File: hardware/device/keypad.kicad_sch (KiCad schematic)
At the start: 49 parts, among them SW1 TRIG1, SW10 TRIG10, SW11 TRIG11, SW12 TRIG12, SW13 TRIG13, SW14 TRIG14, SW15 TRIG15, SW16 TRIG16, SW2 TRIG2, SW3 TRIG3, SW4 TRIG4, SW5 TRIG5, SW6 TRIG6, SW7 TRIG7, SW8 TRIG8, SW9 TRIG9, U10 TRIG9, U11 TRIG13, U12 TRIG10, U13 TRIG14, U14 TRIG11, U15 TRIG15, U16 TRIG12, U17 TRIG16, U2 TRIG1, U25 TCA8418RTWR, U3 TRIG2, U4 TRIG3, U5 TRIG4, U6 TRIG8, U7 TRIG7, U8 TRIG6, U9 TRIG5

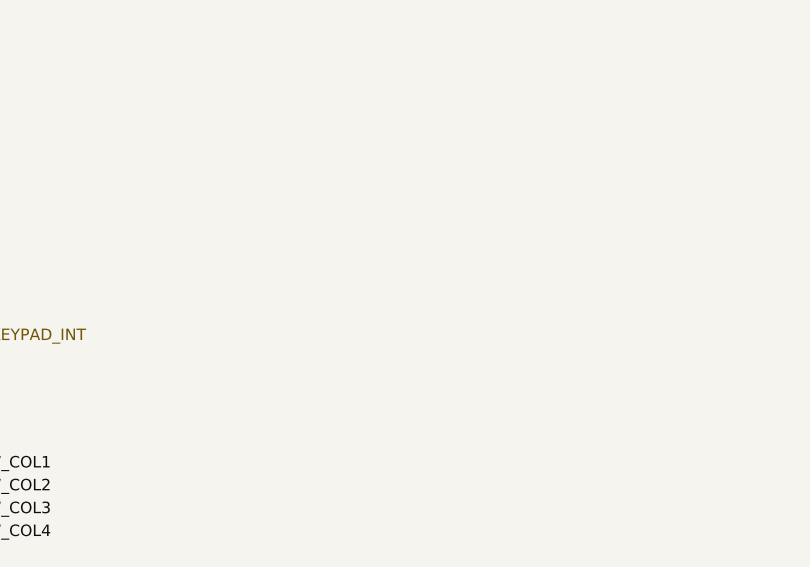
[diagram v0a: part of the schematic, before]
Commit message: feat: project organization, add knob, pcb layout, and 3d models
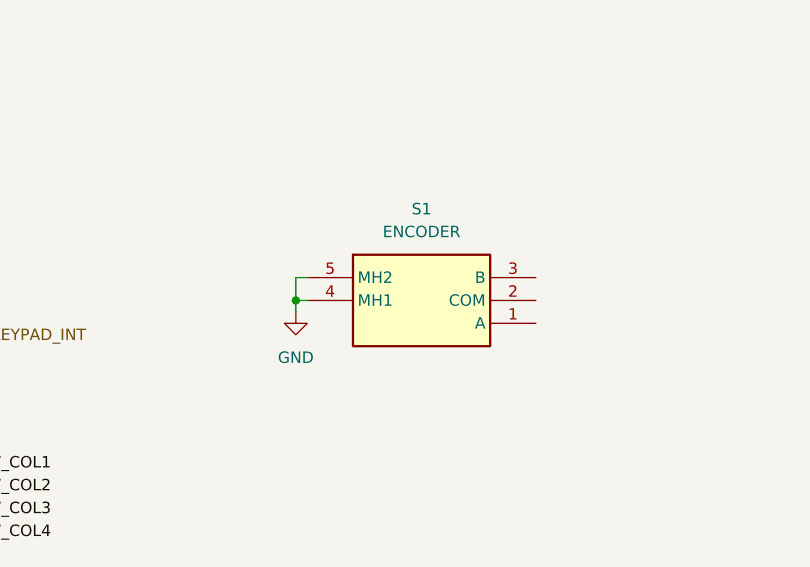
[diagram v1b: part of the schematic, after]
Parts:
- added S1: ENCODER, pocket_synth:2416191-1, symbol pocket_synth:2416191-1
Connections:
- net GND: now also S1.4 (MH1), S1.5 (MH2)

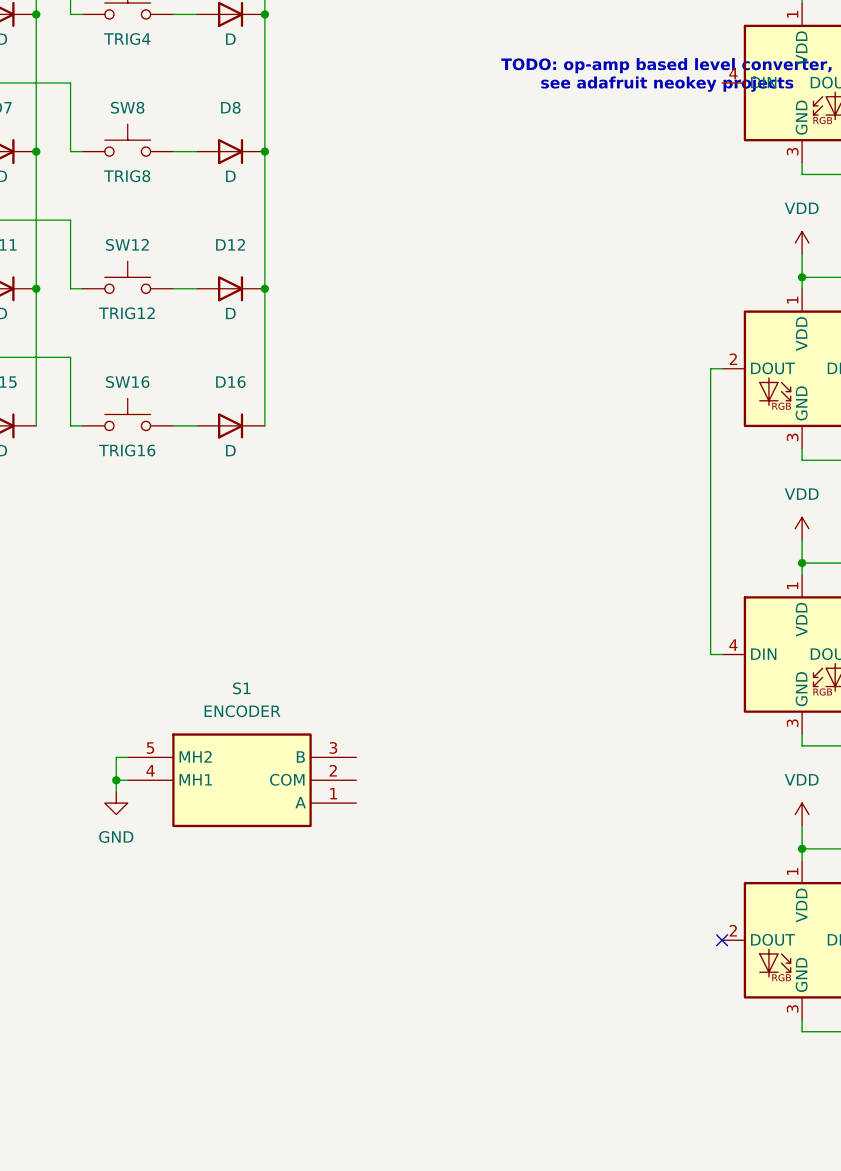
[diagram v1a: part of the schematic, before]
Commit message: feat: various scroll wheel layout changes
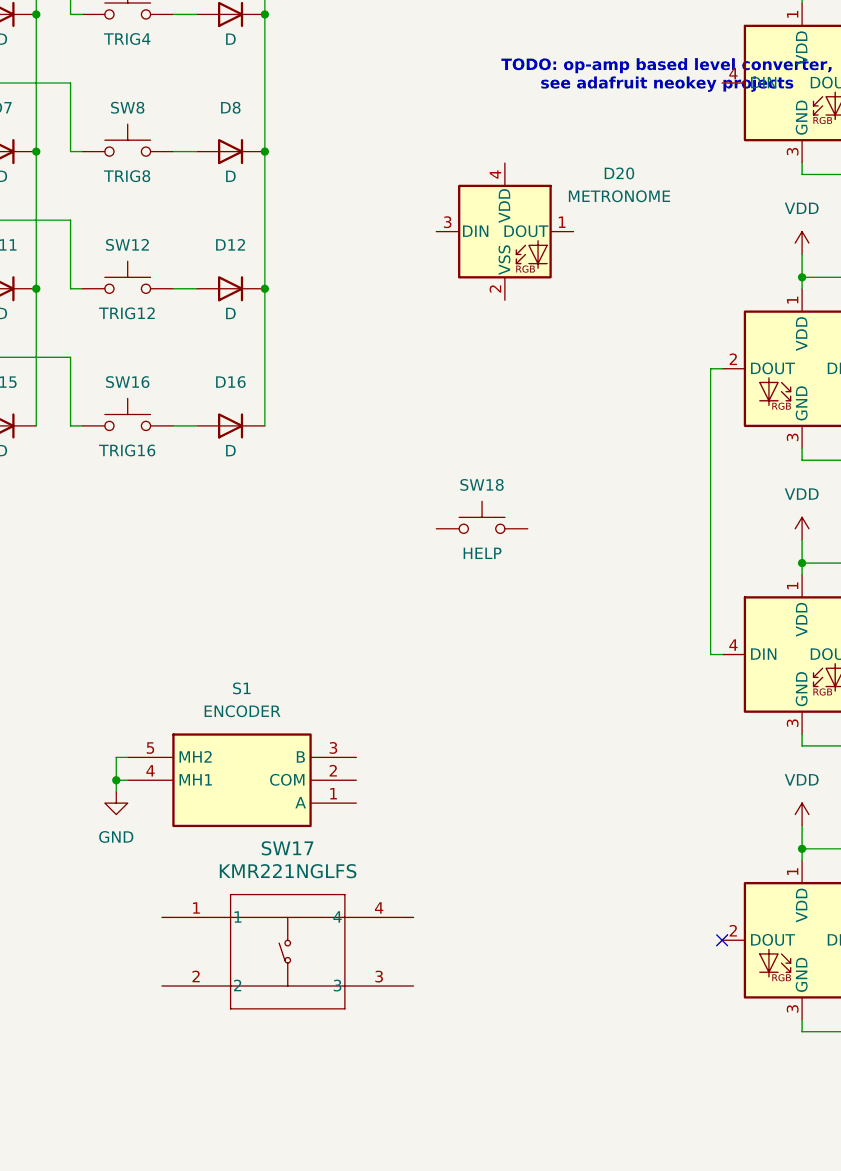
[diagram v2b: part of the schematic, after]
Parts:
- added D20: METRONOME, LED_SMD:LED_SK6812MINI_PLCC4_3.5x3.5mm_P1.75mm, symbol LED:SK6812MINI
- added SW17: KMR221NGLFS, pocket_synth:KMR221_CNK, symbol pocket_synth:KMR221NGLFS
- added SW18: HELP, Button_Switch_SMD:SW_SPST_EVQQ2, symbol Switch:SW_Push
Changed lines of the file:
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@@
+	(symbol
+		(lib_id "Switch:SW_Push")
+		(at 156.21 91.44 0)
+		(unit 1)
+		(exclude_from_sim no)
+		(in_bom yes)
+		(on_board yes)
+		(dnp no)
+		(property "Reference" "SW18"
+			(at 156.21 86.614 0)
+			(effects
+				(font
+					(size 1.27 1.27)
+				)
+			)
+		)
+		(property "Value" "HELP"
+			(at 156.21 93.472 0)
+			(effects
+				(font
+					(size 1.27 1.27)
+				)
+				(justify top)
+			)
+		)
+		(property "Footprint" "Button_Switch_SMD:SW_SPST_EVQQ2"
+			(at 156.21 86.36 0)
+			(effects
+				(font
+					(size 1.27 1.27)
+				)
+				(hide yes)
+			)
+		)
+		(property "Datasheet" "~"
+			(at 156.21 86.36 0)
+			(effects
+				(font
+					(size 1.27 1.27)
+				)
+				(hide yes)
+			)
+		)
+		(property "Description" "Push button switch, generic, two pins"
+			(at 156.21 91.44 0)
+			(effects
+				(font
+					(size 1.27 1.27)
+				)
+				(hide yes)
+			)
+		)
+		(property "JLC" ""
+			(at 156.21 91.44 0)
+			(effects
+				(font
+					(size 1.27 1.27)
+				)
+			)
+		)
+		(pin "1"
+		)
+		(pin "2"
+		)
+		(instances
+			(project "pocket_synth"
+				(path "/485383b8-00f4-4405-b270-de249939cff4/7f1ac839-494f-4521-b63e-5606a3cb7bc9"
+					(reference "SW18")
+					(unit 1)
+				)
+			)
+		)
+	)
 	(symbol
 		(lib_id "Switch:SW_Push")
@@
 	)
 	(symbol
+		(lib_id "LED:SK6812MINI")
+		(at 158.75 58.42 0)
+		(unit 1)
+		(exclude_from_sim no)
+		(in_bom yes)
+		(on_board yes)
+		(dnp no)
+		(fields_autoplaced yes)
+		(property "Reference" "D20"
+			(at 171.45 51.9998 0)
+			(effects
+				(font
+					(size 1.27 1.27)
+				)
+			)
+		)
+		(property "Value" "METRONOME"
+			(at 171.45 54.5398 0)
+			(effects
+				(font
+					(size 1.27 1.27)
+				)
+			)
+		)
+		(property "Footprint" "LED_SMD:LED_SK6812MINI_PLCC4_3.5x3.5mm_P1.75mm"
+			(at 160.02 66.04 0)
+			(effects
+				(font
+					(size 1.27 1.27)
+				)
+				(justify left top)
+				(hide yes)
+			)
+		)
+		(property "Datasheet" "https://cdn-shop.adafruit.com/product-files/2686/SK6812MINI_REV.01-1-2.pdf"
+			(at 161.29 67.945 0)
+			(effects
+				(font
+					(size 1.27 1.27)
+				)
+				(justify left top)
+				(hide yes)
+			)
+		)
+		(property "Description" "RGB LED with integrated controller"
+			(at 158.75 58.42 0)
+			(effects
+				(font
+					(size 1.27 1.27)
+				)
+				(hide yes)
+			)
+		)
+		(pin "3"
+		)
+		(pin "4"
+		)
+		(pin "2"
+		)
+		(pin "1"
+		)
+		(instances
+			(project ""
+				(path "/485383b8-00f4-4405-b270-de249939cff4/7f1ac839-494f-4521-b63e-5606a3cb7bc9"
+					(reference "D20")
+					(unit 1)
+				)
+			)
+		)
+	)
+	(symbol
 		(lib_id "power:VDD")
 		(at 191.77 29.21 0)
@@
 					(unit 1)
 				)
+			)
+		)
+	)
+	(symbol
+		(lib_id "pocket_synth:KMR221NGLFS")
+		(at 120.65 134.62 0)
+		(unit 1)
+		(exclude_from_sim no)
+		(in_bom yes)
+		(on_board yes)
+		(dnp no)
+		(fields_autoplaced yes)
+		(property "Reference" "SW17"
+			(at 134.62 127 0)
+			(effects
+				(font
+					(size 1.524 1.524)
+				)
+			)
+		)
+		(property "Value" "KMR221NGLFS"
+			(at 134.62 129.54 0)
+			(effects
+				(font
+					(size 1.524 1.524)
+				)
+			)
+		)
+		(property "Footprint" "pocket_synth:KMR221_CNK"
+			(at 120.65 134.62 0)
+			(effects
+				(font
+					(size 1.27 1.27)
+					(italic yes)
+				)
+				(hide yes)
+			)
+		)
+		(property "Datasheet" "KMR221NGLFS"
+			(at 120.65 134.62 0)
+			(effects
+				(font
+					(size 1.27 1.27)
+					(italic yes)
+				)
+				(hide yes)
+			)
+		)
+		(property "Description" ""
+			(at 120.65 134.62 0)
+			(effects
+				(font
+					(size 1.27 1.27)
+				)
+				(hide yes)
+			)
+		)
+		(pin "2"
+		)
+		(pin "4"
+		)
+		(pin "3"
+		)
+		(pin "1"
+		)
+		(instances
+			(project ""
+				(path "/485383b8-00f4-4405-b270-de249939cff4/7f1ac839-494f-4521-b63e-5606a3cb7bc9"
+					(reference "SW17")
+					(unit 1)
+				)

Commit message: feat: various layouts, changed SDRAM to BGA
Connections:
- net I2C.SDA: now reaches U25.22 (SDA)
- net I2C.SCL: now reaches U25.23 (SCL)
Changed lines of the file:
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@@
 		(at 182.88 137.16)
 	)
+	(bus_entry
+		(at 25.4 130.81)
+		(size -2.54 -2.54)
+		(stroke
+			(width 0)
+			(type default)
+		)
+	)
+	(bus_entry
+		(at 25.4 128.27)
+		(size -2.54 -2.54)
+		(stroke
+			(width 0)
+			(type default)
+		)
+	)
 	(wire
 		(pts
@@
 		)
 	)
+	(bus
+		(pts
+			(xy 22.86 120.65) (xy 22.86 125.73)
+		)
+		(stroke
+			(width 0)
+			(type default)
+		)
+	)
 	(wire
 		(pts
@@
 		)
 	)
+	(bus
+		(pts
+			(xy 22.86 125.73) (xy 22.86 128.27)
+		)
+		(stroke
+			(width 0)
+			(type default)
+		)
+	)
 	(wire
 		(pts
@@
 	(wire
 		(pts
+			(xy 25.4 130.81) (xy 41.91 130.81)
+		)
+		(stroke
+			(width 0)
+			(type default)
+		)
+	)
+	(wire
+		(pts
 			(xy 214.63 83.82) (xy 237.49 83.82)
 		)
@@
 	(wire
 		(pts
+			(xy 25.4 128.27) (xy 41.91 128.27)
+		)
+		(stroke
+			(width 0)
+			(type default)
+		)
+	)
+	(wire
+		(pts
 			(xy 59.69 72.39) (xy 85.09 72.39)
 		)
@@
 		)
 	)
-	(label "SW_ROW1"
-		(at 30.48 26.67 180)
+	(label "I2C.SCL"
+		(at 40.64 128.27 180)
 		(effects
 			(font
@@
 	)
 	(label "SW_ROW1"
-		(at 39.37 138.43 180)
+		(at 30.48 26.67 180)
 		(effects
 			(font
@@
 		)
 	)
-	(label "SW_ROW4"
-		(at 39.37 146.05 180)
+	(label "SW_ROW1"
+		(at 39.37 138.43 180)
 		(effects
 			(font
@@
 		)
 	)
+	(label "SW_ROW4"
+		(at 39.37 146.05 180)
+		(effects
+			(font
+				(size 1.27 1.27)
+			)
+			(justify right bottom)
+		)
+	)
+	(label "I2C.SDA"
+		(at 40.64 130.81 180)
+		(effects
+			(font
+				(size 1.27 1.27)
+			)
+			(justify right bottom)
+		)
+	)
 	(label "SW_COL1"
 		(at 80.01 138.43 0)
@@
 		(effects
 			(font
+				(size 1.27 1.27)
+			)
+			(justify left)
+		)
+	)
+	(hierarchical_label "{I2C}"
+		(shape input)
+		(at 22.86 120.65 90)
+		(effects
+			(font

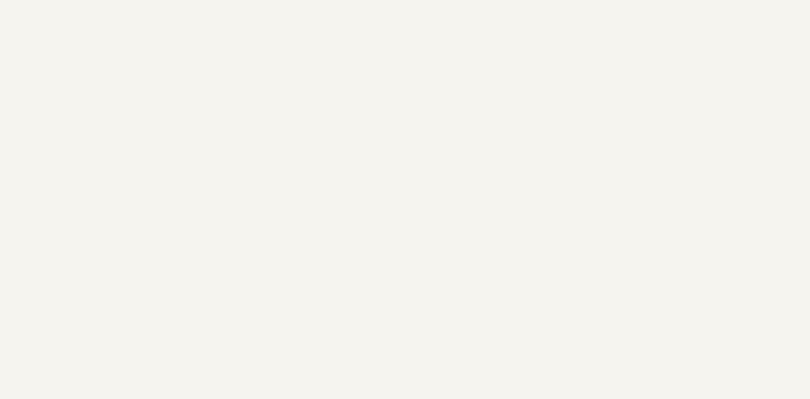
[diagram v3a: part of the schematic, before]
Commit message: feat: various PCB layout and routing
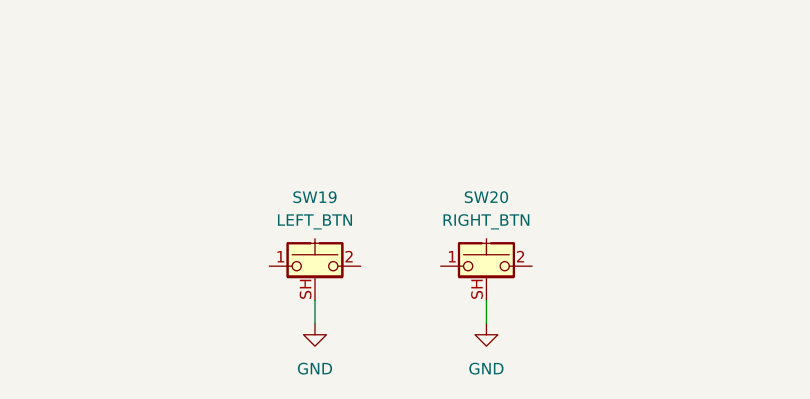
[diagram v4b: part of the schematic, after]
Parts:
- added SW19: LEFT_BTN, Button_Switch_SMD:SW_Push_1P1T-MP_NO_Horizontal_Alps_SKRTLAE010, symbol Switch:SW_Push_Shielded
- added SW20: RIGHT_BTN, Button_Switch_SMD:SW_Push_1P1T-MP_NO_Horizontal_Alps_SKRTLAE010, symbol Switch:SW_Push_Shielded
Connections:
- net GND: now also SW19.SH (B), SW20.SH (B)

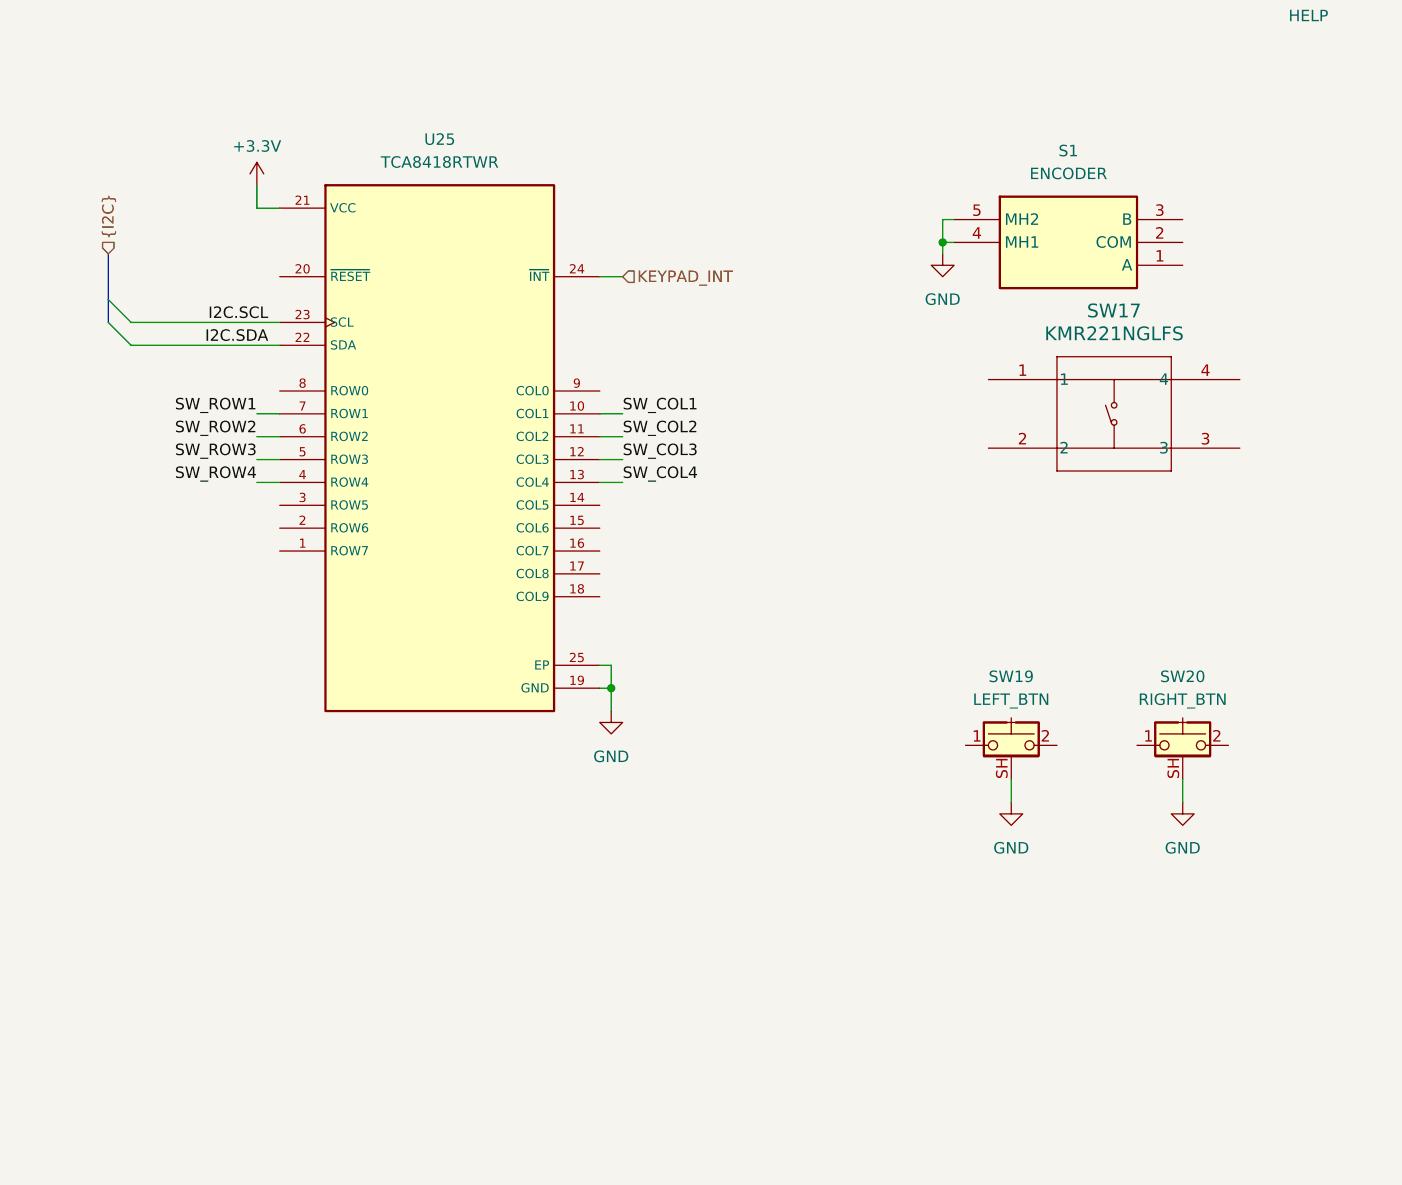
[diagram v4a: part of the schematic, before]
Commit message: feat: add audio routing muxes
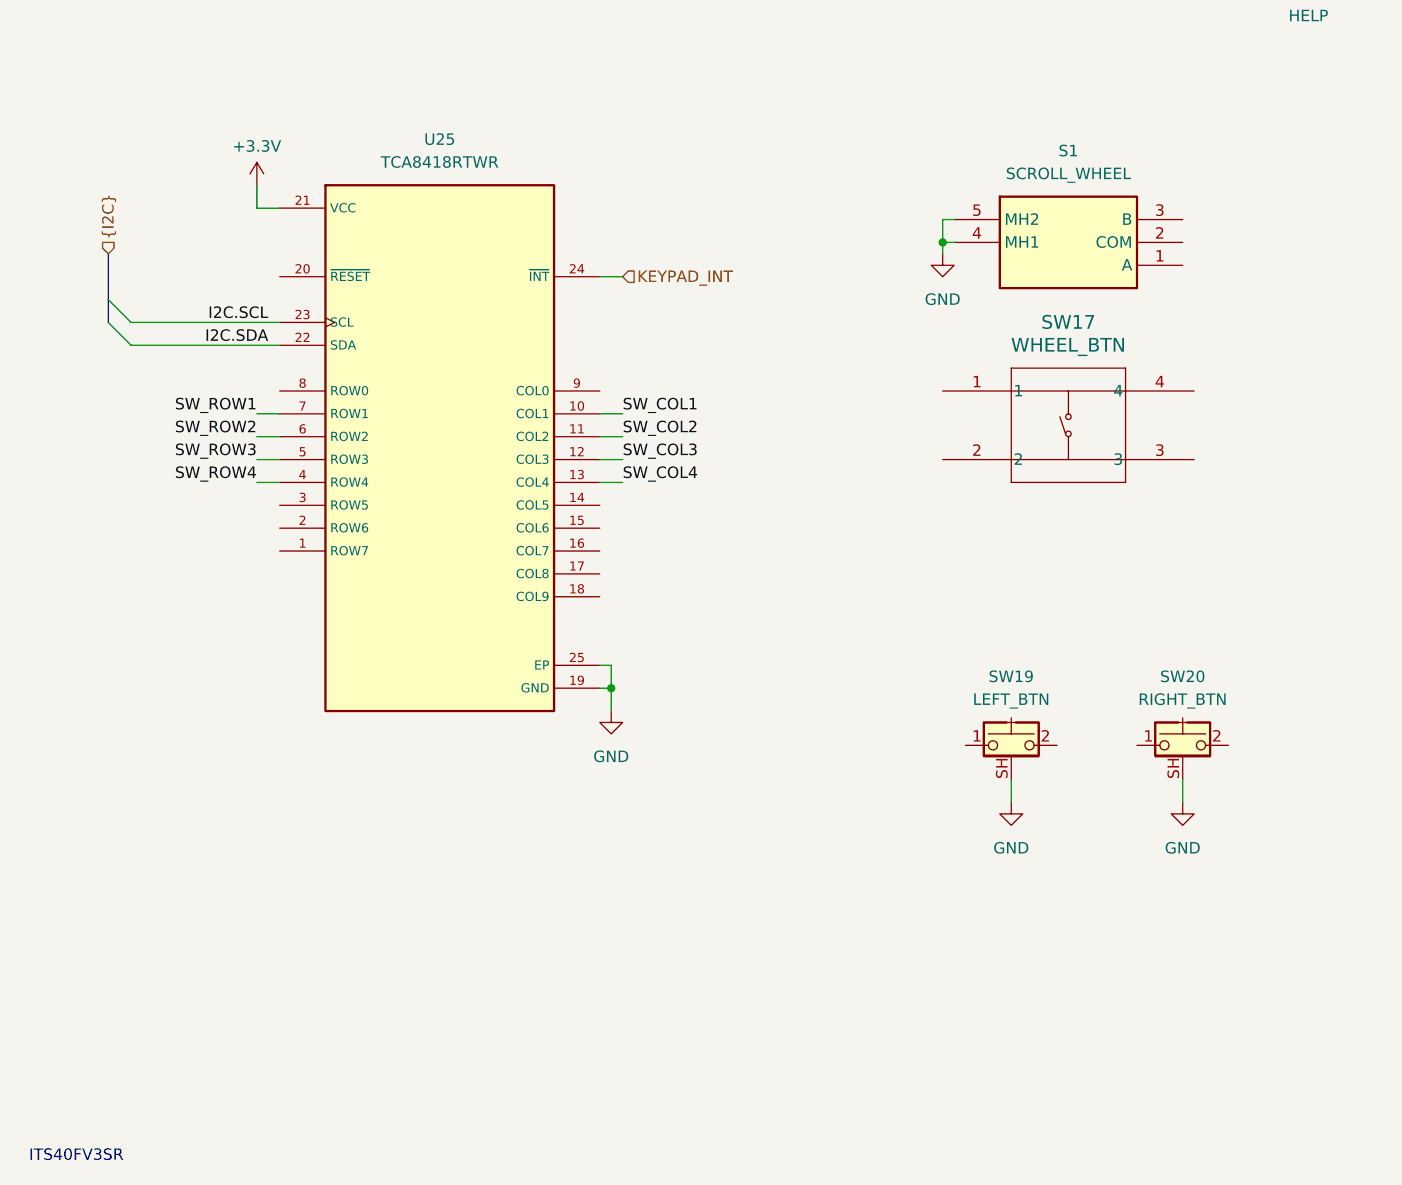
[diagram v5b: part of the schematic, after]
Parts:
- S1: value ENCODER -> SCROLL_WHEEL
- SW17: value KMR221NGLFS -> WHEEL_BTN
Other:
- note added: "ITS40FV3SR"
- moved on the sheet: SW17
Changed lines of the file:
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@@
 		)
 	)
+	(text "ITS40FV3SR"
+		(exclude_from_sim no)
+		(at 19.304 220.98 0)
+		(effects
+			(font
+				(size 1.27 1.27)
+			)
+		)
+	)
 	(junction
 		(at 34.29 26.67)
@@
 			)
 		)
-		(property "Value" "ENCODER"
+		(property "Value" "SCROLL_WHEEL"
 			(at 129.54 111.76 0)
 			(effects
@@
 	(symbol
 		(lib_id "pocket_synth:KMR221NGLFS")
-		(at 120.65 134.62 0)
+		(at 115.57 135.89 0)
 		(unit 1)
 		(exclude_from_sim no)
@@
 		(fields_autoplaced yes)
 		(property "Reference" "SW17"
-			(at 134.62 127 0)
+			(at 129.54 128.27 0)
 			(effects
 				(font
@@
 			)
 		)
-		(property "Value" "KMR221NGLFS"
-			(at 134.62 129.54 0)
+		(property "Value" "WHEEL_BTN"
+			(at 129.54 130.81 0)
 			(effects
 				(font
@@
 		)
 		(property "Footprint" "pocket_synth:KMR221_CNK"
-			(at 120.65 134.62 0)
+			(at 115.57 135.89 0)
 			(effects
 				(font
@@
 		)
 		(property "Datasheet" "KMR221NGLFS"
-			(at 120.65 134.62 0)
+			(at 115.57 135.89 0)
 			(effects
 				(font
@@
 		)
 		(property "Description" ""
-			(at 120.65 134.62 0)
+			(at 115.57 135.89 0)
 			(effects
 				(font
